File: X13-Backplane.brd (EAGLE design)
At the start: 160 x 100 mm, 45 parts, among them J2 284512-4, J3 284512-8, J4 284512-8, J5 284512-4, Y1 ECS-80-S-4X

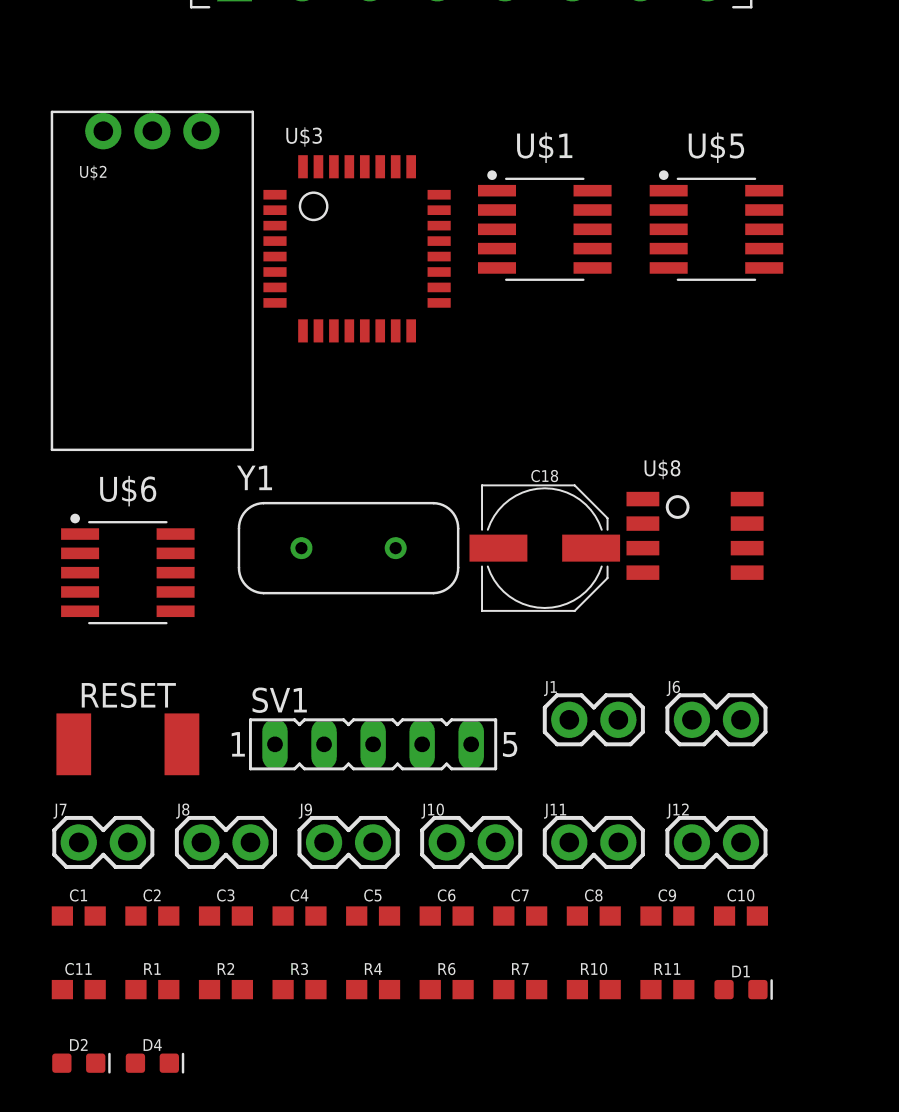
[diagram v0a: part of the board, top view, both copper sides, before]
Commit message: Updated Solenoid Board
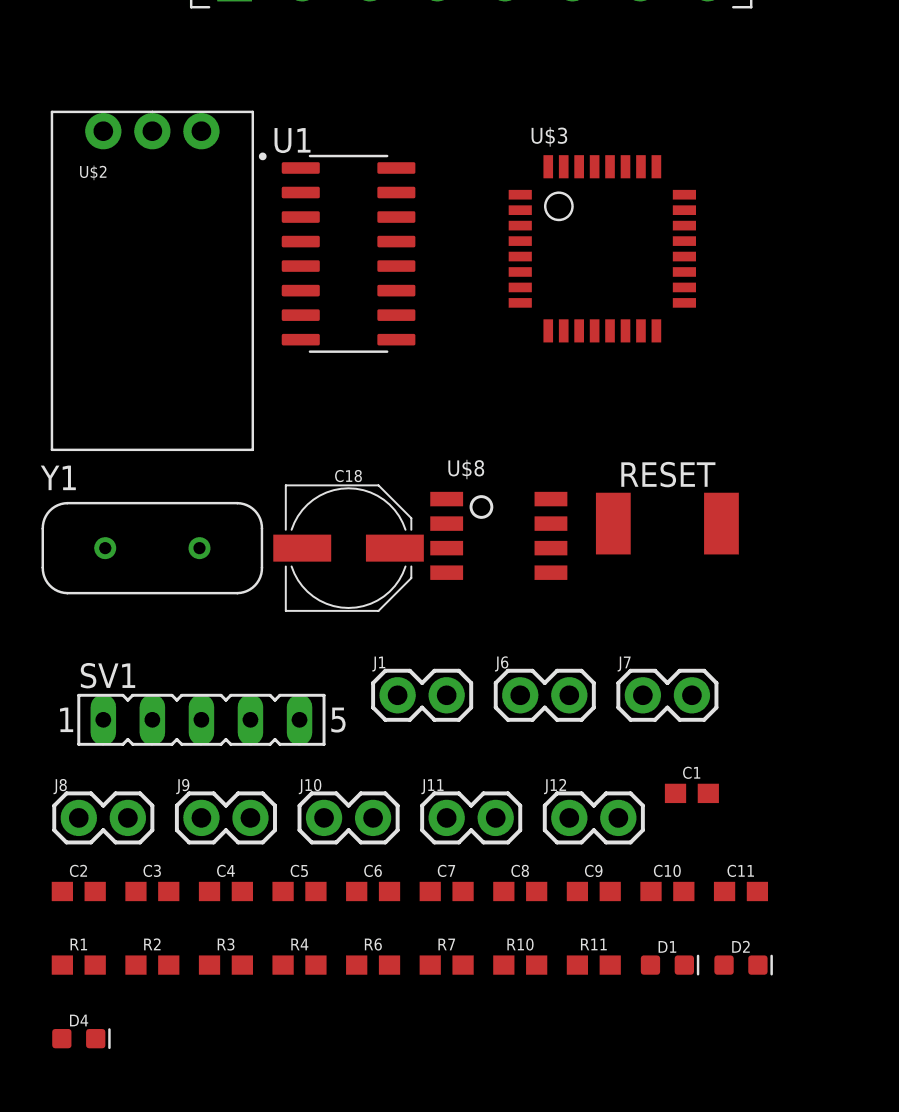
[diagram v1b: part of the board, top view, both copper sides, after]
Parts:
- removed U$1, U$5, U$6: LV8548M, HBridge:SOP100P600X175-10N
- added U1: ULN2003V12, ULN2003V12:ULN2003V12
- moved C11 34.7 mm to (-14.0, -40.6)
- moved D2 34.7 mm to (-14.0, -44.5)
- moved C1 32.4 mm to (-16.5, -35.6)
- moved RESET 30.2 mm to (-17.8, -21.6)
- moved J7 30.2 mm to (-19.1, -30.5)
- moved U$3 12.7 mm to (-25.4, -10.2)
- moved Y1 10.2 mm to (-44.5, -22.9)
- moved C18 10.2 mm to (-34.3, -22.9)
- moved U$8 10.2 mm to (-29.2, -24.1)
- moved J1 8.98 mm to (-31.8, -30.5)
- moved J6 8.98 mm to (-25.4, -30.5)
- moved SV1 8.98 mm to (-41.9, -31.8)
- moved J10 6.48 mm to (-35.6, -36.8)
- moved J11 6.48 mm to (-29.2, -36.8)
- moved J8 6.48 mm to (-48.3, -36.8)
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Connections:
- removed net GPIO0: U$1.IN4, U$3.PB7
- removed net SOL1_2: J1.1, U$1.OUT2
- removed net SOL2_2: J6.1, U$1.OUT4
- removed net SOL3_2: J7.1, U$5.OUT2
- removed net SOL4_2: J8.1, U$5.OUT4
- removed net SOL5_2: J9.1, U$6.OUT2
- removed net SOL6_2: J10.1, U$6.OUT4
- new net ALERT: U$3.PB7
- new net CLK: U$3.PA9
- new net DATA: U$3.PA10
- net 12V: now also J1.1, J10.1, J6.1, J7.1, J8.1, J9.1, U1.9; no longer U$1.VCC, U$5.VCC, U$6.VCC
- net GND: now also U1.8; no longer U$1.GND, U$5.GND, U$6.GND
- net GPIO1: now also U1.4; no longer U$1.IN3
- net GPIO10: now also U1.3; no longer U$5.IN3
- net GPIO11: now also U1.2; no longer U$5.IN4
- net GPIO12: now also U1.1; no longer U$6.IN1
- net GPIO13: no longer U$6.IN2
- net GPIO14: now also U$3.PA1; no longer U$3.PA9, U$6.IN3
- net GPIO15: now also U$3.PA0; no longer U$3.PA10, U$6.IN4
- net GPIO2: now also U1.5; no longer U$1.IN2
- net GPIO3: now also U1.6; no longer U$1.IN1
- net GPIO8: no longer U$5.IN1
- net GPIO9: no longer U$5.IN2
- net SOL1_1: now also U1.16; no longer U$1.OUT1
- net SOL2_1: now also U1.15; no longer U$1.OUT3
- net SOL3_1: now also U1.14; no longer U$5.OUT1
- net SOL4_1: now also U1.13; no longer U$5.OUT3
- net SOL5_1: now also U1.12; no longer U$6.OUT1
- net SOL6_1: now also U1.11; no longer U$6.OUT3

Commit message: added Thrusters/motor connectors + QuadESC Connectors
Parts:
- removed C18: 47uF, SparkFun-Capacitors:PANASONIC_D
- removed J12: (no value), SparkFun-Connectors:1X02
- added MC1, MC2, MC3, MC4, T1, T2, T3, T4, T5, T6, T7, T8: 284512-3, ThrusterConnector:284512-3
- added U$1, U$4, U$5, U$6, U$7: ESC2BACKPLANE, ESC_to_Backplane_Connectors:ESC2BACKPLANE_WHOLE
- J11: value (none) -> 284512-8; device SparkFun-Connectors:1X02 -> 284512-8:TE_284512-8
- U$2: value MURATA-DC-DC -> ESC2BACKPLANE; device MURATA_3pin_dcdc:MURATA-DC-DC -> ESC_to_Backplane_Connectors:ESC2BACKPLANE_WHOLE
- moved D2 190.8 mm to (-97.8, 127.0)
- moved D1 187.6 mm to (-94.0, 127.0)
- moved R11 185.8 mm to (-90.2, 128.3)
- moved D4 183.2 mm to (-101.6, 127.0)
- moved R10 183.2 mm to (-86.4, 128.3)
- moved R7 180.8 mm to (-82.5, 128.3)
- moved R6 178.7 mm to (-78.7, 128.3)
- moved R4 176.9 mm to (-74.9, 128.3)
- moved R3 175.4 mm to (-71.1, 128.3)
- moved J9 175.0 mm to (-125.7, 116.8)
- moved C11 175.0 mm to (-59.7, 128.3)
- moved J7 174.7 mm to (-113.0, 116.8)
- moved R2 174.2 mm to (-67.3, 128.3)
- moved R1 173.4 mm to (-63.5, 128.3)
- moved C10 173.2 mm to (-55.9, 128.3)
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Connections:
- new net ESC-ID_1: U$7.P$8
- new net ESC-ID_2: U$5.P$8
- new net ESC-ID_3: U$2.P$8
- new net MC1_PHS1: MC1.P$1
- new net MC1_PHS2: MC1.P$2
- new net MC1_PHS3: MC1.P$3
- new net MC2_PHS1: MC2.P$1
- new net MC2_PHS2: MC2.P$2
- new net MC2_PHS3: MC2.P$3
- new net MC3_PHS1: MC3.P$1
- new net MC3_PHS2: MC3.P$2
- new net MC3_PHS3: MC3.P$3
- new net MC4_PHS1: MC4.P$1
- new net MC4_PHS2: MC4.P$2
- new net MC4_PHS3: MC4.P$3
- new net SWCLK_4: MUX.11, U$3.PA14
- new net SWDIO_4: MUX.4, U$3.PA13
- new net T1_PHS1: T1.P$1
- new net T1_PHS2: T1.P$2
- new net T1_PHS3: T1.P$3
- new net T2_PHS1: T2.P$1
- new net T2_PHS2: T2.P$2
- new net T2_PHS3: T2.P$3
- new net T3_PHS1: T3.P$1
- new net T3_PHS2: T3.P$2
- new net T3_PHS3: T3.P$3
- new net T4_PHS1: T4.P$1
- new net T4_PHS2: T4.P$2
- new net T4_PHS3: T4.P$3
- new net T5_PHS1: T5.P$1
- new net T5_PHS2: T5.P$2
- new net T5_PHS3: T5.P$3
- new net T6_PHS1: T6.P$1
- new net T6_PHS2: T6.P$2
- new net T6_PHS3: T6.P$3
- new net T7_PHS1: T7.P$1
- new net T7_PHS2: T7.P$2
- new net T7_PHS3: T7.P$3
- new net T8_PHS1: T8.P$1
- new net T8_PHS2: T8.P$2
- new net T8_PHS3: T8.P$3
- net +3V3: now also J11.5; no longer J3.5, U$2.3
- net 12V: now also U$1.P$A, U$1.P$B, U$1.P$C, U$1.P$D, U$1.P$E, U$1.P$O, U$1.P$P, U$1.P$Q, U$1.P$R, U$1.P$S, U$2.P$10, U$2.P$11, U$2.P$12, U$2.P$13, U$2.P$23, U$2.P$24, U$2.P$25, U$2.P$26, U$2.P$27, U$2.P$9, U$4.P$A, U$4.P$B, U$4.P$C, U$4.P$D, U$4.P$E, U$4.P$O, U$4.P$P, U$4.P$Q, U$4.P$R, U$4.P$S, U$5.P$10, U$5.P$11, U$5.P$12, U$5.P$13, U$5.P$23, U$5.P$24, U$5.P$25, U$5.P$26, U$5.P$27, U$5.P$9, U$6.P$A, U$6.P$B, U$6.P$C, U$6.P$D, U$6.P$E, U$6.P$O, U$6.P$P, U$6.P$Q, U$6.P$R, U$6.P$S, U$7.P$10, U$7.P$11, U$7.P$12, U$7.P$13, U$7.P$23, U$7.P$24, U$7.P$25, U$7.P$26, U$7.P$27, U$7.P$9; no longer C18.+, J11.2, U$2.1
- net 3.3V: now also J3.5, U$1.P$G, U$1.P$H, U$1.P$U, U$1.P$V, U$4.P$G, U$4.P$H, U$4.P$U, U$4.P$V, U$6.P$G, U$6.P$H, U$6.P$U, U$6.P$V
- net CAN_H: now also U$2.P$6, U$5.P$6, U$7.P$6; no longer J12.2
- net CAN_L: now also U$2.P$7, U$5.P$7, U$7.P$7; no longer J12.1
- net GND: now also U$1.P$AA, U$1.P$BB, U$1.P$J, U$1.P$K, U$1.P$L, U$1.P$M, U$1.P$N, U$1.P$X, U$1.P$Y, U$1.P$Z, U$2.P$1, U$2.P$15, U$2.P$16, U$2.P$17, U$2.P$18, U$2.P$2, U$2.P$3, U$2.P$4, U$4.P$AA, U$4.P$BB, U$4.P$J, U$4.P$K, U$4.P$L, U$4.P$M, U$4.P$N, U$4.P$X, U$4.P$Y, U$4.P$Z, U$5.P$1, U$5.P$15, U$5.P$16, U$5.P$17, U$5.P$18, U$5.P$2, U$5.P$3, U$5.P$4, U$6.P$AA, U$6.P$BB, U$6.P$J, U$6.P$K, U$6.P$L, U$6.P$M, U$6.P$N, U$6.P$X, U$6.P$Y, U$6.P$Z, U$7.P$1, U$7.P$15, U$7.P$16, U$7.P$17, U$7.P$18, U$7.P$2, U$7.P$3, U$7.P$4; no longer C18.-, U$2.2
- net NRST: now also J11.6, U$2.P$20, U$5.P$20, U$7.P$20
- net PROG_1: now also J11.2, U$7.P$5
- net PROG_2: now also J11.3, U$5.P$5
- net PROG_3: now also J11.4, U$2.P$5
- net SWCLK: no longer U$3.PA14
- net SWCLK_1: now also U$7.P$22
- net SWCLK_2: now also U$5.P$22
- net SWCLK_3: now also U$2.P$22
- net SWCLK_IN: now also J11.7
- net SWDIO: no longer U$3.PA13
- net SWDIO_1: now also U$7.P$21
- net SWDIO_2: now also U$5.P$21
- net SWDIO_3: now also U$2.P$21
- net SWDIO_IN: now also J11.8

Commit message: Design review changes-2
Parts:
- removed J10, J6, J7, J8, J9: (no value), SparkFun-Connectors:1X02
- added J12: 284512-8, 284512-8:TE_284512-8
- added R5: 26.7k, SparkFun-Resistors:0603
- added R8: 10k, SparkFun-Resistors:0603
- added R9: 5k, SparkFun-Resistors:0603
- J1: value (none) -> 284512-4; device SparkFun-Connectors:1X02 -> 284512-4:TE_284512-4
- R10, R11: value 60 -> 1k
- moved J1 305.2 mm to (-116.8, -188.0)
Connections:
- new net GPIO0: U$3.PA2
- new net N$3: R5.1
- new net N$4: R8.1
- net +3V3: no longer C1.1, C2.1, C3.1, C4.1, C5.1, C6.1, J11.5, R2.2, R6.2, SV1.5, U$3.VDD, U$3.VDDA, U$3.VDDIO2
- net 12V: now also J12.7; no longer J1.1, J10.1, J6.1, J7.1, J8.1, J9.1
- net 3.3V: now also C1.1, C2.1, C3.1, C4.1, C5.1, C6.1, J11.5, R2.2, R6.2, SV1.5, U$3.VDD, U$3.VDDA, U$3.VDDIO2
- net 5V: now also J1.1, J1.2
- net ESC-ID_1: now also R5.2
- net ESC-ID_2: now also R8.2
- net ESC-ID_3: now also R9.2
- net GND: now also J1.3, J1.4, R9.1
- net SOL1_1: now also J12.1; no longer J1.2
- net SOL2_1: now also J12.2; no longer J6.2
- net SOL3_1: now also J12.3; no longer J7.2
- net SOL4_1: now also J12.4; no longer J8.2
- net SOL5_1: now also J12.5; no longer J9.2
- net SOL6_1: now also J12.6; no longer J10.2
- net SWDIO_IN: now also J12.8

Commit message: added LED resistor values
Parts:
- R4, R6: value (none) -> 470
- R5: value 26.7k -> 22k
- R9: value 5k -> 4.7k
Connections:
- removed net N$4: R8.1
- net GND: now also R8.1
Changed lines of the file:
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@@
 <attribute name="VALUE" x="-71.12" y="127.508" size="0.6096" layer="27" font="vector" ratio="20" align="top-center"/>
 </element>
-<element name="R4" library="SparkFun-Resistors" library_urn="urn:adsk.eagle:library:532" package="0603" package3d_urn="urn:adsk.eagle:package:39650/1" value=" " x="-74.93" y="128.27" smashed="yes">
+<element name="R4" library="SparkFun-Resistors" library_urn="urn:adsk.eagle:library:532" package="0603" package3d_urn="urn:adsk.eagle:package:39650/1" value="470" x="-74.93" y="128.27" smashed="yes">
 <attribute name="NAME" x="-74.93" y="129.032" size="0.6096" layer="25" font="vector" ratio="20" align="bottom-center"/>
 <attribute name="PROD_ID" value=" " x="0" y="0" size="1.778" layer="27" display="off"/>
 <attribute name="VALUE" x="-74.93" y="127.508" size="0.6096" layer="27" font="vector" ratio="20" align="top-center"/>
 </element>
-<element name="R6" library="SparkFun-Resistors" library_urn="urn:adsk.eagle:library:532" package="0603" package3d_urn="urn:adsk.eagle:package:39650/1" value=" " x="-78.74" y="128.27" smashed="yes">
+<element name="R6" library="SparkFun-Resistors" library_urn="urn:adsk.eagle:library:532" package="0603" package3d_urn="urn:adsk.eagle:package:39650/1" value="470" x="-78.74" y="128.27" smashed="yes">
 <attribute name="NAME" x="-78.74" y="129.032" size="0.6096" layer="25" font="vector" ratio="20" align="bottom-center"/>
 <attribute name="PROD_ID" value=" " x="0" y="0" size="1.778" layer="27" display="off"/>
@@
 <attribute name="VALUE" x="-126.54" y="-192.61" size="1.27" layer="27"/>
 </element>
-<element name="R5" library="SparkFun-Resistors" library_urn="urn:adsk.eagle:library:532" package="0603" package3d_urn="urn:adsk.eagle:package:39650/1" value="26.7k" x="-125.73" y="-195.58" smashed="yes">
+<element name="R5" library="SparkFun-Resistors" library_urn="urn:adsk.eagle:library:532" package="0603" package3d_urn="urn:adsk.eagle:package:39650/1" value="22k" x="-125.73" y="-195.58" smashed="yes">
 <attribute name="NAME" x="-125.73" y="-194.818" size="0.6096" layer="25" font="vector" ratio="20" align="bottom-center"/>
 <attribute name="PROD_ID" value="RES-12186" x="-125.73" y="-195.58" size="1.778" layer="27" display="off"/>
@@
 <attribute name="VALUE" x="-125.73" y="-200.152" size="0.6096" layer="27" font="vector" ratio="20" align="top-center"/>
 </element>
-<element name="R9" library="SparkFun-Resistors" library_urn="urn:adsk.eagle:library:532" package="0603" package3d_urn="urn:adsk.eagle:package:39650/1" value="5k" x="-125.73" y="-203.2" smashed="yes">
+<element name="R9" library="SparkFun-Resistors" library_urn="urn:adsk.eagle:library:532" package="0603" package3d_urn="urn:adsk.eagle:package:39650/1" value="4.7k" x="-125.73" y="-203.2" smashed="yes">
 <attribute name="NAME" x="-125.73" y="-202.438" size="0.6096" layer="25" font="vector" ratio="20" align="bottom-center"/>
 <attribute name="PROD_ID" value="RES-07856" x="-125.73" y="-203.2" size="1.778" layer="27" display="off"/>
@@
 <contactref element="J1" pad="4"/>
 <contactref element="R9" pad="1"/>
+<contactref element="R8" pad="1"/>
 <wire x1="-121.92" y1="-123.19" x2="-124.46" y2="-123.19" width="0" layer="19" extent="1-1"/>
 <wire x1="-124.46" y1="-120.65" x2="-124.46" y2="-123.19" width="0" layer="19" extent="1-1"/>
@@
 <wire x1="-115.09" y1="-187.96" x2="-116.84" y2="-123.19" width="0" layer="19" extent="1-1"/>
 <wire x1="-111.59" y1="-187.96" x2="-115.09" y2="-187.96" width="0" layer="19" extent="1-1"/>
-<wire x1="-126.58" y1="-203.2" x2="-115.09" y2="-187.96" width="0" layer="19" extent="1-1"/>
+<wire x1="-126.58" y1="-199.39" x2="-115.09" y2="-187.96" width="0" layer="19" extent="1-1"/>
+<wire x1="-126.58" y1="-203.2" x2="-126.58" y2="-199.39" width="0" layer="19" extent="1-1"/>
 <wire x1="-116.84" y1="-44.45" x2="-102.87" y2="-114.3" width="0" layer="19" extent="1-1"/>
 <wire x1="-119.38" y1="-44.45" x2="-116.84" y2="-44.45" width="0" layer="19" extent="1-1"/>
@@
 <contactref element="R5" pad="1"/>
 </signal>
-<signal name="N$4">
-<contactref element="R8" pad="1"/>
-</signal>
 </signals>

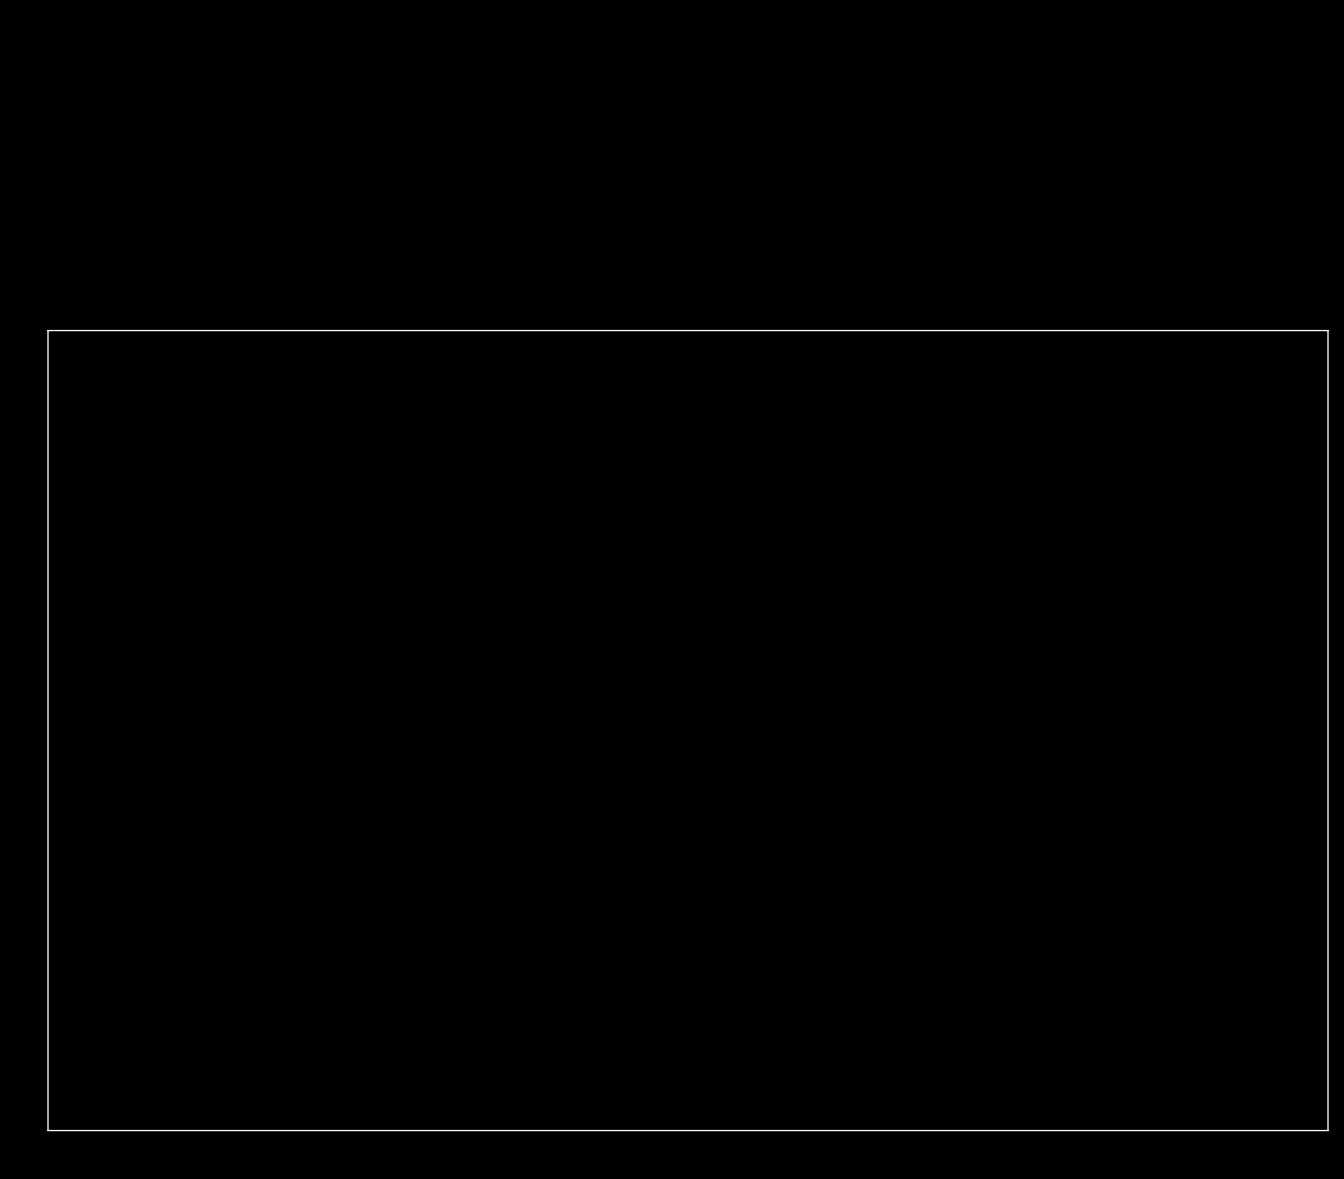
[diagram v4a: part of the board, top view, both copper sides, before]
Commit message: board dimension
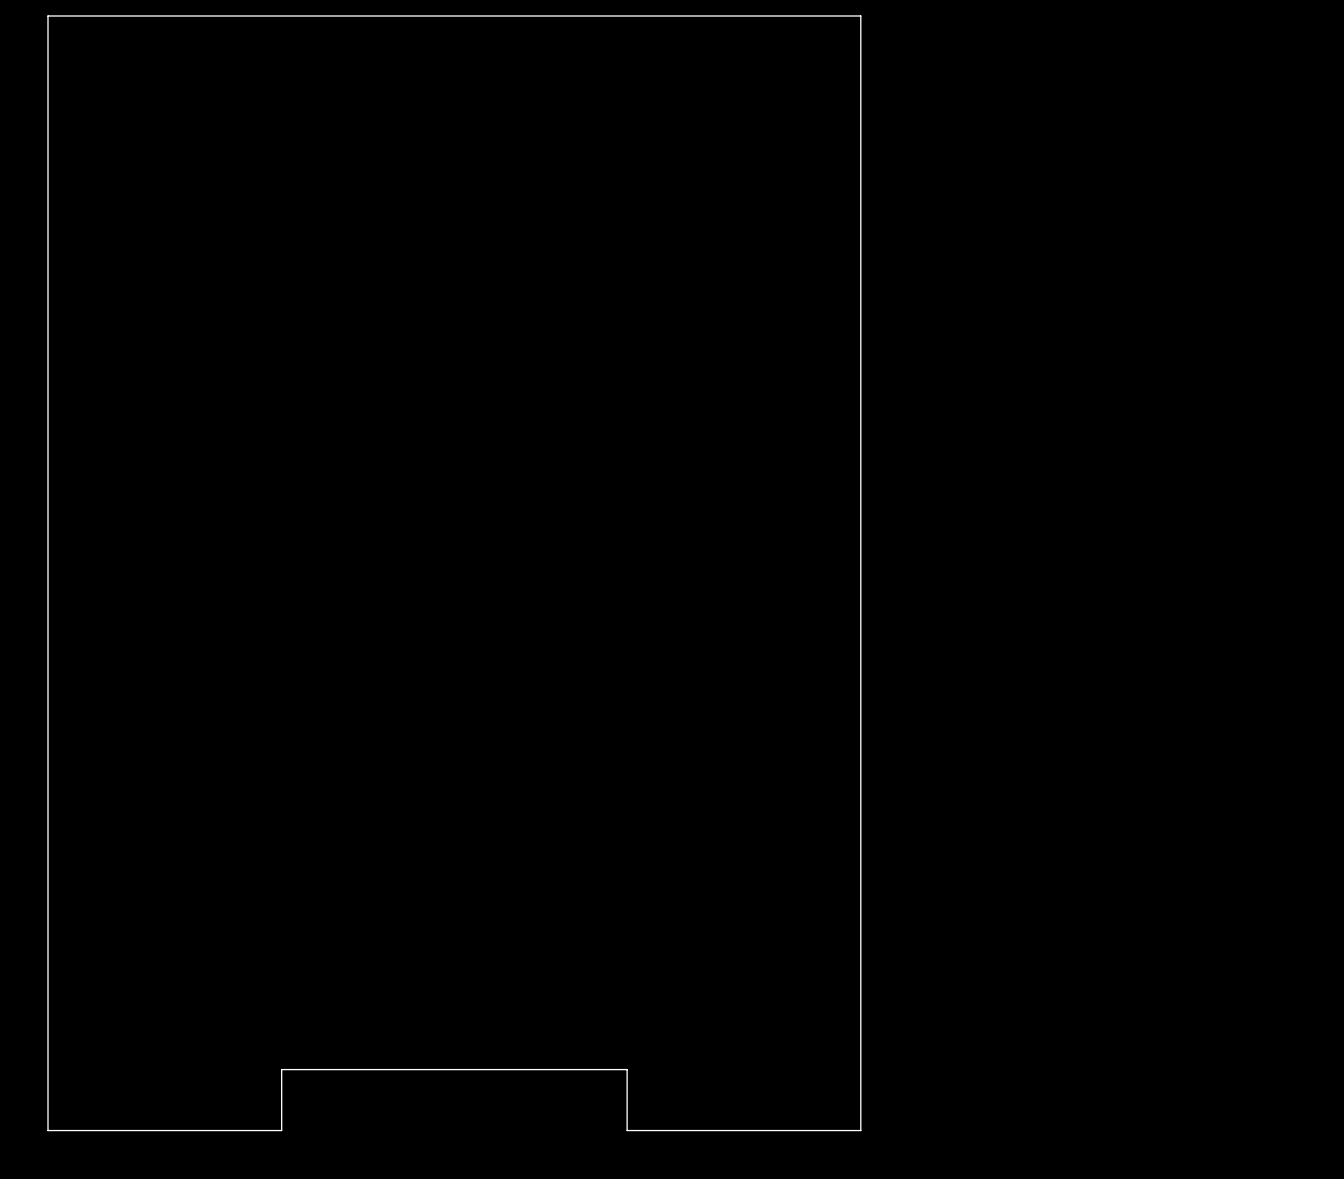
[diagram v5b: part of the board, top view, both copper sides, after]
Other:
- board size 160 x 100 mm -> 101.6 x 139.3 mm
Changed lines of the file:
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@@
 <board>
 <plain>
-<wire x1="0" y1="0" x2="160" y2="0" width="0" layer="20"/>
-<wire x1="160" y1="0" x2="160" y2="100" width="0" layer="20"/>
-<wire x1="160" y1="100" x2="0" y2="100" width="0" layer="20"/>
-<wire x1="0" y1="100" x2="0" y2="0" width="0" layer="20"/>
+<wire x1="0" y1="0" x2="29.21" y2="0" width="0" layer="20"/>
+<wire x1="72.39" y1="0" x2="101.6" y2="0" width="0" layer="20"/>
+<wire x1="101.6" y1="0" x2="101.6" y2="139.319" width="0" layer="20"/>
+<wire x1="101.6" y1="139.319" x2="0" y2="139.319" width="0" layer="20"/>
+<wire x1="0" y1="139.319" x2="0" y2="0" width="0" layer="20"/>
+<wire x1="29.21" y1="7.62" x2="29.21" y2="0" width="0" layer="20"/>
+<wire x1="29.21" y1="7.62" x2="72.39" y2="7.62" width="0" layer="20"/>
+<wire x1="72.39" y1="7.62" x2="72.39" y2="0" width="0" layer="20"/>
 </plain>
 <attributes>
